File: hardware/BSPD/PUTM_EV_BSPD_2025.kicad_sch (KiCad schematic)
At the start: 27 parts, among them K1 Fujitsu_FTR-LYCA005x, Q1 NMOS, U1 MC78M12CDTG, U10 4069, U2 LM1117IMP-5.0, U4 Opamp_Dual, U5 4081

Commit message: Crumbs of documentation added
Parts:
- R1: value R -> 10k
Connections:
- net at C7.1, R18.2, R19.1: no longer U10.1
- net SCS Loop but the other side: now reaches K1.11
- net SCS Loop: now reaches K1.14
- no-connect marks 0 -> 3
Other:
- note added: "(Labels will be changed to not idiotic)"
- note added: "...eventually"
- note added: "0.5V-4.5V Output Comparator"
- note added: "A nice little graph of trigger times + voltages will be added"
- note added: "Comparator will be added here"
- note added: "Timing Section 500ms Charge 10s Discharge"
- moved on the sheet: C7, R18, R19, R3, R5, U10A, U5A

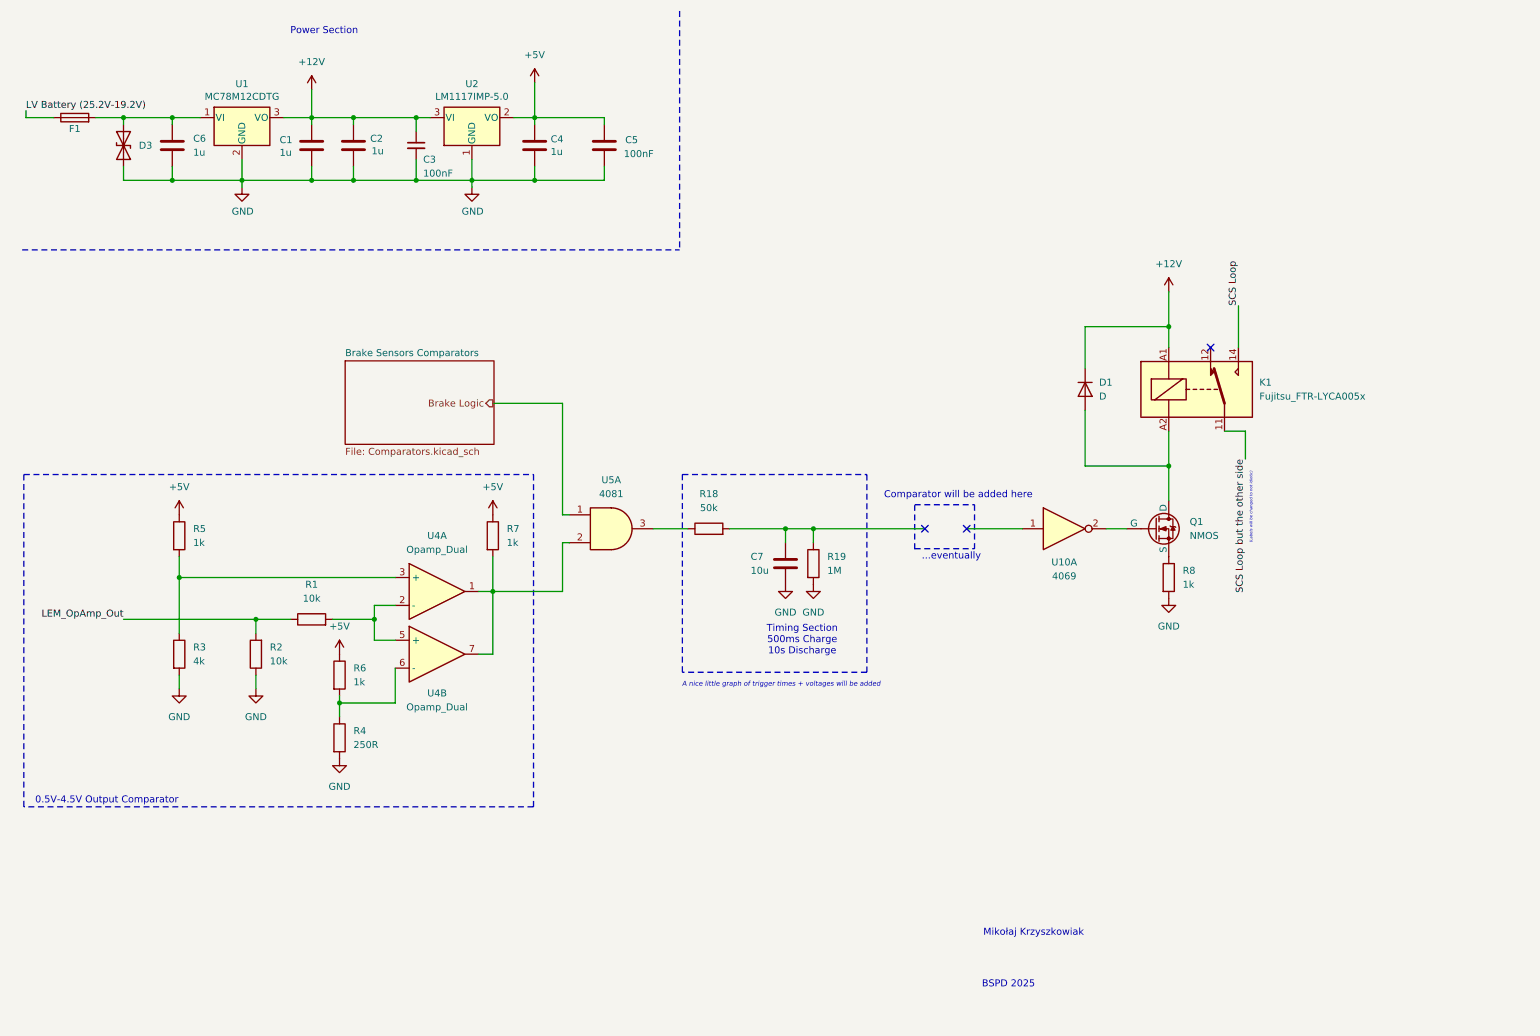
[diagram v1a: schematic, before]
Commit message: Timing Changed + Documented
Changed 10 second autoreset timer to a 555 in one-shot configuration. Also documented BSPD Board.
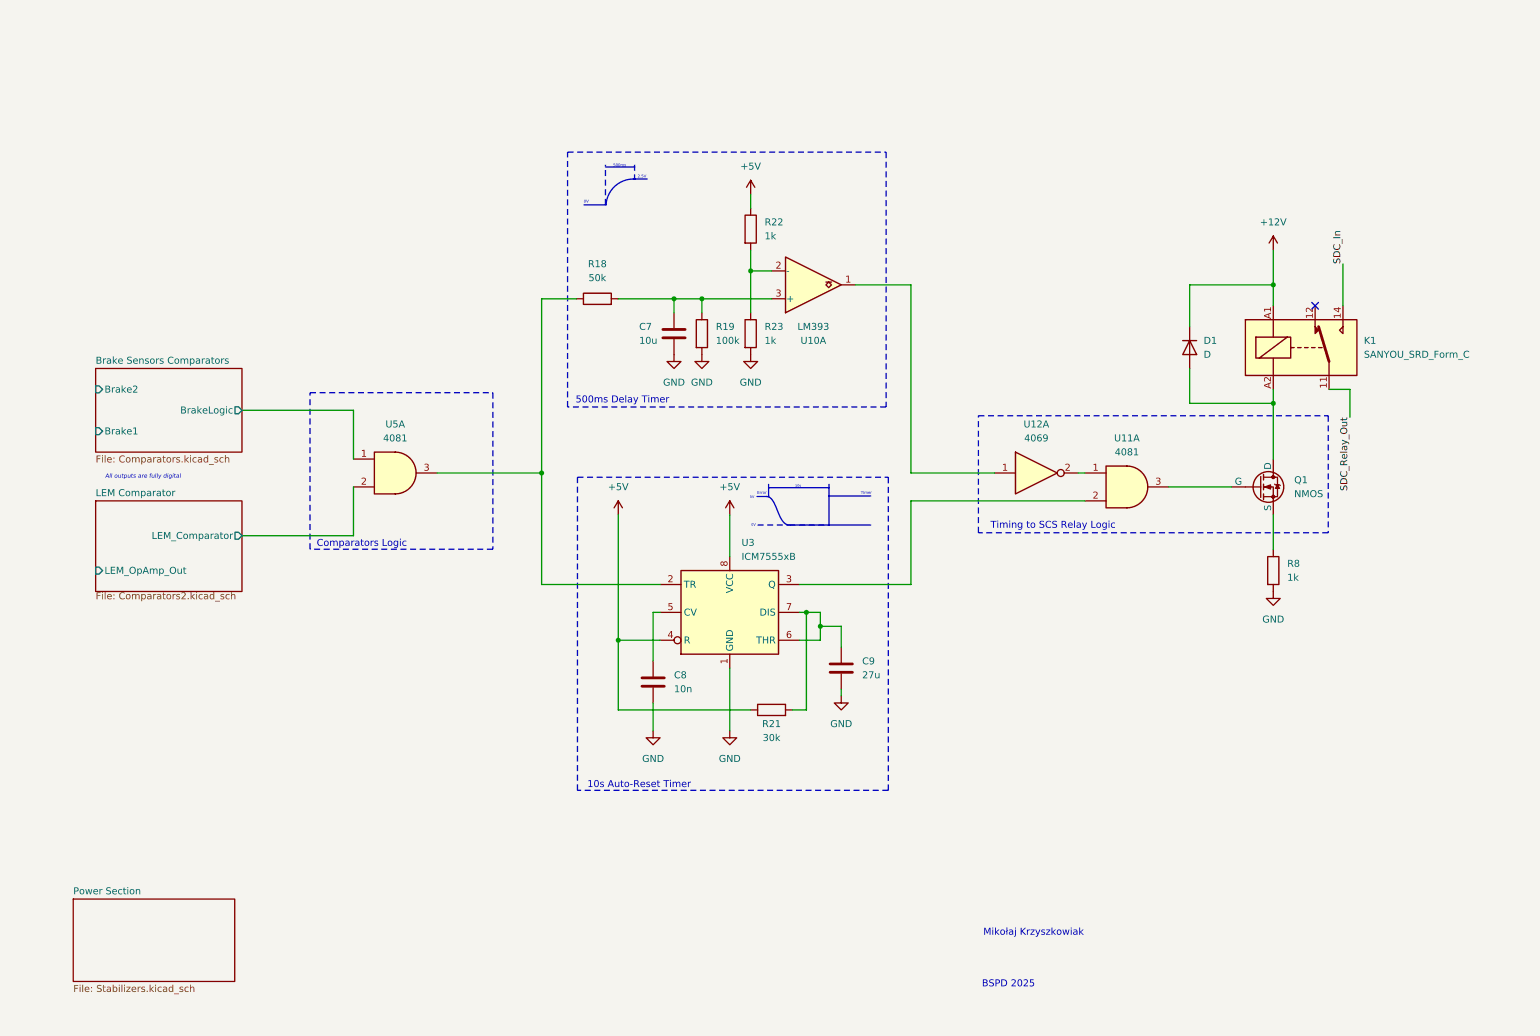
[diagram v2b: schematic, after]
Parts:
- removed C1, C2, C4: 1u, Capacitor_SMD:C_0805_2012Metric, symbol PUTM_EV_IMD_SAFETY_2021-rescue:C-Device
- removed C3: 100nF, Capacitor_SMD:C_0603_1608Metric, symbol Device:C_Small
- removed C5: 100nF, Capacitor_SMD:C_0603_1608Metric, symbol PUTM_EV_IMD_SAFETY_2021-rescue:C-Device
- removed C6: 1u, symbol Device:C
- removed D3: 1N630xCA, Diode_THT:D_DO-201AE_P15.24mm_Horizontal, symbol Diode:1N630xCA
- removed F1: 500mA, symbol Device:Fuse
- removed R1: 10k, symbol Device:R
- removed R2: 10k, Resistor_SMD:R_1206_3216Metric, symbol Device:R
- removed R3: 4k, symbol Device:R
- removed R4: 250R, symbol Device:R
- removed R5, R6, R7: 1k, symbol Device:R
- removed U1: MC78M12CDTG, Package_TO_SOT_SMD:TO-252-3_TabPin2, symbol PUTM_EV_IMD_SAFETY_2021-rescue:MC78M05_TO252-Regulator_Linear
- removed U10: 4069, symbol 4xxx:4069
- removed U2: LM1117IMP-5.0, Package_TO_SOT_SMD:SOT-223-3_TabPin2, symbol PUTM_EV_IMD_SAFETY_2021-rescue:LM1117-5.0-Regulator_Linear
- removed U4: Opamp_Dual, symbol Device:Opamp_Dual
- added C8: 10n, symbol Device:C
- added C9: 27u, symbol Device:C
- added R21: 30k, symbol Device:R
- added R22, R23: 1k, symbol Device:R
- added U10: LM393, symbol Comparator:LM393
- added U11: 4081, symbol 4xxx:4081
- added U12: 4069, symbol 4xxx:4069
- added U3: ICM7555xB, Package_SO:SOIC-8_3.9x4.9mm_P1.27mm, symbol Timer:ICM7555xB
- K1: value Fujitsu_FTR-LYCA005x -> SANYOU_SRD_Form_C
- R19: value 1M -> 100k
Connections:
- net +5V: now also R21.1, R22.1, U3.4 (R), U3.8 (VCC)
- net GND: now also C8.2, C9.2, R23.2, U3.1 (GND)
- net at C7.1, R18.2, R19.1: now also U10.3 (+)
- net at R18.1, U5.3: now also U3.2 (TR)
- net at Q1.2 (G): now also U11.3
- net LEM Comparator/LEM_Comparator: now reaches U5.2
- net Brake Logic renamed Brake Sensors Comparators/BrakeLogic
- net SCS Loop renamed SDC_In
- net SCS Loop but the other side renamed SDC_Relay_Out
- new net: R22.2, R23.1, U10.2 (-)
- new net: C9.1, R21.2, U3.6 (THR), U3.7 (DIS)
- new net: U11.2, U3.3 (Q)
- new net: C8.1, U3.5 (CV)
- new net: U10.1, U12.1
- new net: U11.1, U12.2
- no-connect marks 3 -> 1
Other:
- added sheet LEM Comparator (Comparators2.kicad_sch)
- added sheet Power Section (Stabilizers.kicad_sch)
- sheet Brake Sensors Comparators ports: added Brake1, Brake2, BrakeLogic; removed none
- note added: "0V"
- note added: "10s"
- note added: "10s Auto-Reset Timer"
- note added: "2.5V"
- note added: "500ms"
- note added: "500ms Delay Timer"
- note added: "5V"
- note added: "All outputs are fully digital"
- note added: "Comparators Logic"
- note added: "Error"
- note added: "Timer"
- note added: "Timing to SCS Relay Logic"
- note removed: "(Labels will be changed to not idiotic)"
- note removed: "...eventually"
- note removed: "0.5V-4.5V Output Comparator"
- note removed: "A nice little graph of trigger times + voltages will be added"
- note removed: "Comparator will be added here"
- note removed: "Power Section"
- note removed: "Timing Section 500ms Charge 10s Discharge"
- moved on the sheet: C7, D1, K1, Q1, R18, R19, R8, U5A

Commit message: Minor documentation + schematic changes
Changed documentation to more descriptive, fixed zajebas where OpAmps were placed instead of comparators. 
Changed resistors values on CS board
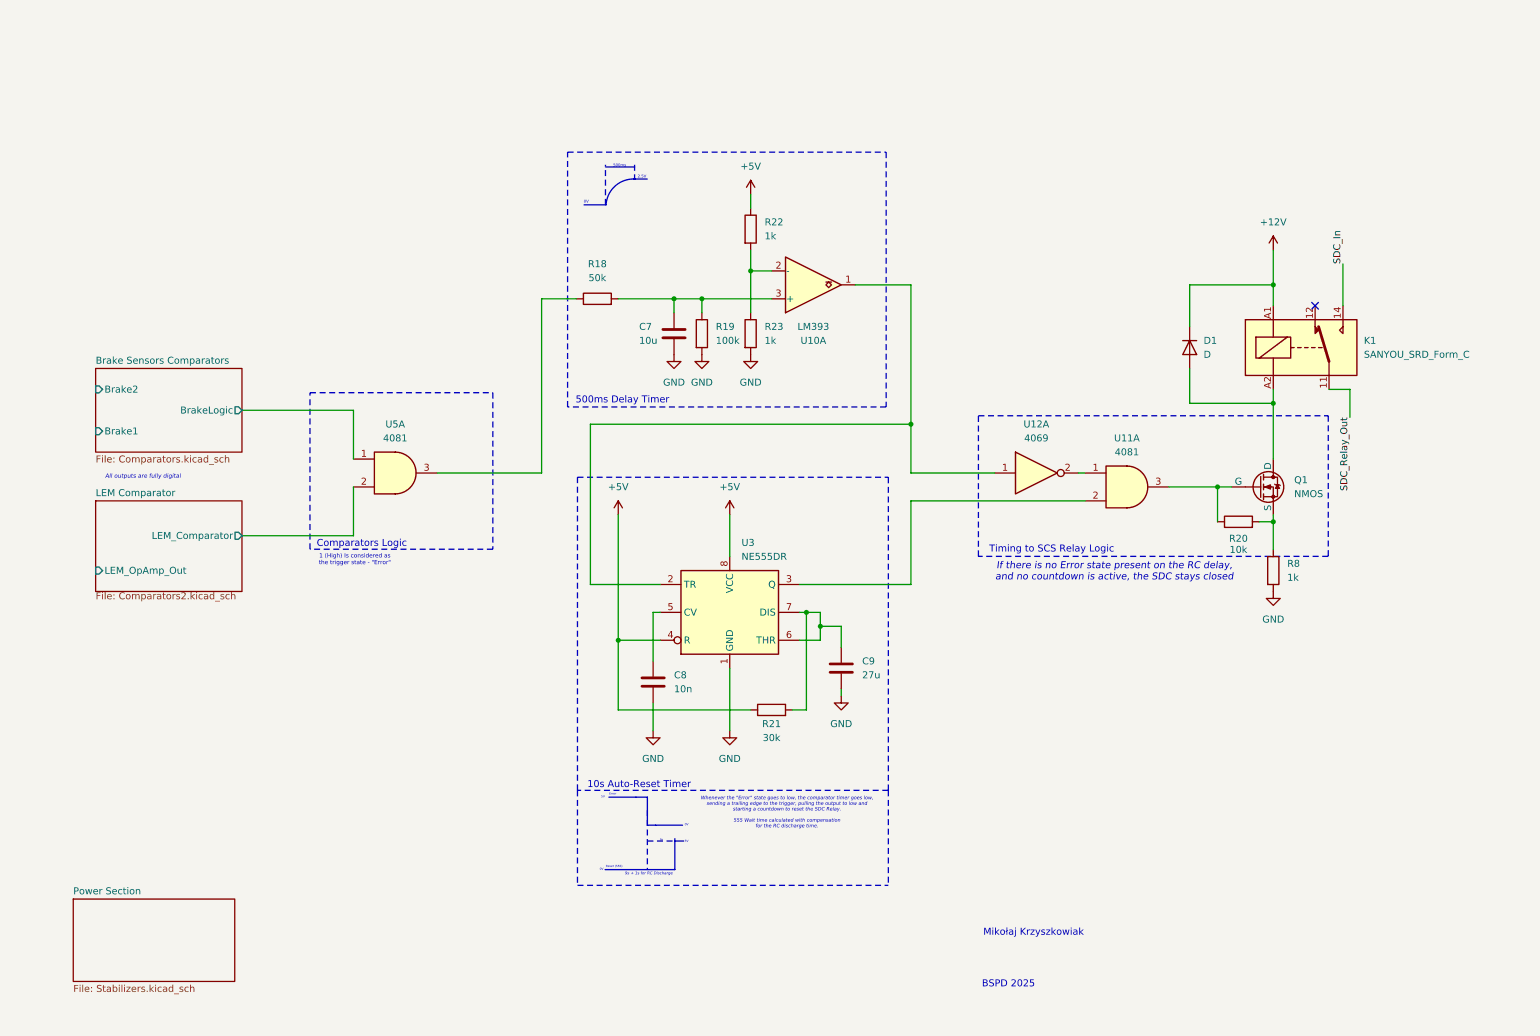
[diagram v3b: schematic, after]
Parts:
- added R20: 10k, symbol Device:R
- U3: value ICM7555xB -> NE555DR
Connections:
- net at R18.1, U5.3: no longer U3.2 (TR)
- net at U10.1, U12.1: now also U3.2 (TR)
- net at Q1.2 (G), U11.3: now also R20.1
- net at Q1.3 (S), R8.1: now also R20.2
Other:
- note added: "1 (High) Is considered as the trigger state - "Error""
- note added: "9s"
- note added: "9s + 1s for RC Discharge"
- note added: "If there is no Error state present on the RC delay, and no countdown is active, the SDC stays closed"
- note added: "Reset (555)"
- note added: "Whenever the "Error" state goes to low, the comparator timer goes low, sending a trailing edge to the trigger, pulling the output to low and starting a countdown to reset the SDC Relay. 555 Wait time calculated with compensation for the RC discharge time."
- note removed: "10s"
- note removed: "Timer"

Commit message: Fixed logic errors + assigned element values
Fixed wrong logic on Brake Sensor comparators, assigned IC's and connectors, added TVS diodes on connectors.
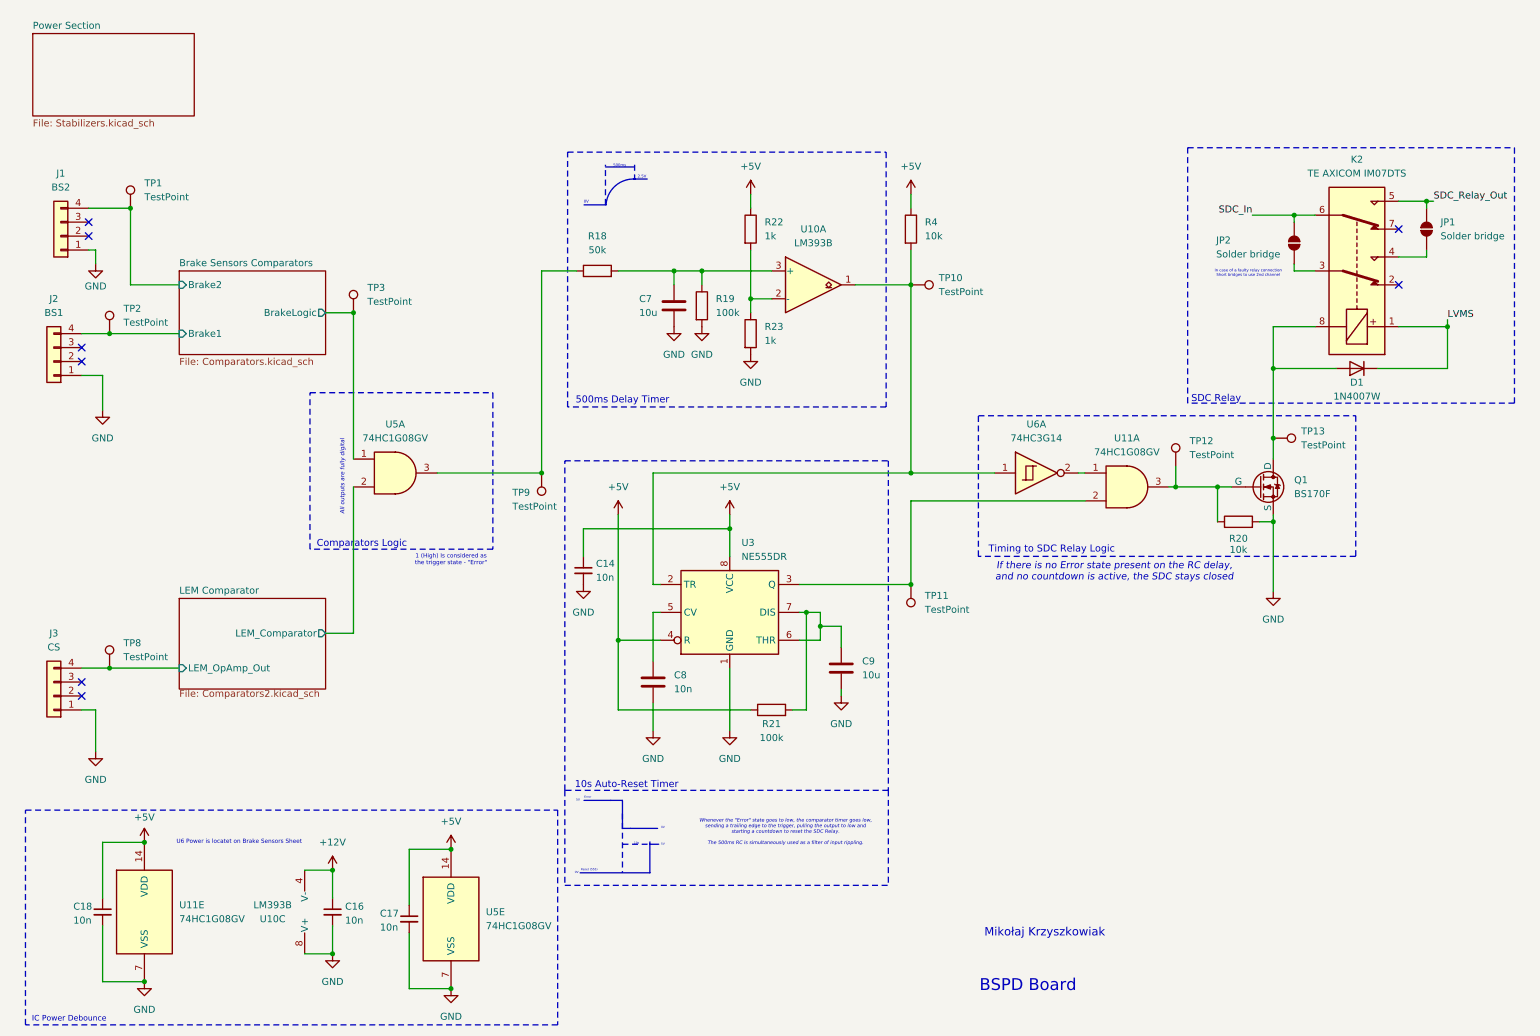
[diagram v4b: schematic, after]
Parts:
- removed K1: SANYOU_SRD_Form_C, Relay_THT:Relay_SPDT_Fujitsu_FTR-LYCA005x_FormC_Vertical, symbol Relay:Fujitsu_FTR-LYCA005x
- removed R8: 1k, symbol Device:R
- removed U12: 4069, symbol 4xxx:4069
- added C14, C16, C17, C18: 10n, symbol Device:C_Small
- added J1: BS2, symbol Connector_Generic:Conn_01x04
- added J2: BS1, symbol Connector_Generic:Conn_01x04
- added J3: CS, symbol Connector_Generic:Conn_01x04
- added JP1, JP2: Solder bridge, symbol Jumper:SolderJumper_2_Open
- added K2: TE AXICOM IM07DTS, footprints:IM23TS, symbol Relay:IM07
- added R4: 10k, symbol Device:R
- added TP1, TP10, TP11, TP12, TP13, TP2, TP3, TP8, TP9: TestPoint, symbol Connector:TestPoint
- added unit 3 of U10
- added unit 5 of U11
- added unit 5 of U5
- added U6: 74HC3G14, symbol 74xx:74HC14
- C9: value 27u -> 10u
- D1: value D -> 1N4007W
- Q1: value NMOS -> BS170F
- R21: value 30k -> 100k
- U10: value LM393 -> LM393B
- U11, U5: value 4081 -> 74HC1G08GV
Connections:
- net +12V: now also C16.1, U10.4 (V-); no longer D1.1 (K)
- net +5V: now also C14.1, C17.1, C18.1, R4.1, U11.14 (VDD), U5.14 (VDD)
- net Brake Sensors Comparators/Brake1: now also J2.4 (Pin_4), TP2.1
- net Brake Sensors Comparators/Brake2: now also J1.4 (Pin_4), TP1.1
- net Brake Sensors Comparators/BrakeLogic: now also TP3.1
- net GND: now also Q1.3 (S), R20.2, C14.2, C16.2, C17.2, C18.2, J1.1 (Pin_1), J2.1 (Pin_1), J3.1 (Pin_1), U10.8 (V+), U11.7 (VSS), U5.7 (VSS)
- net LEM Comparator/LEM_OpAmp_Out: now also J3.4 (Pin_4), TP8.1
- net SDC_In: now also JP2.2 (B), K2.6
- net SDC_Relay_Out: now also JP1.2 (B), K2.5
- net at Q1.2 (G), R20.1, U11.3: now also TP12.1
- net at R18.1, U5.3: now also TP9.1
- net at U10.1, U3.2 (TR): now also R4.2, TP10.1, U6.1
- net at U11.2, U3.3 (Q): now also TP11.1
- net at U11.1: now also U6.2
- net at D1.2 (A), Q1.1 (D): now also K2.8, TP13.1
- new net: JP2.1 (A), K2.3
- new net: JP1.1 (A), K2.4
- new net LVMS: D1.1 (K), K2.1
- no-connect marks 1 -> 8
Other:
- note added: "10s"
- note added: "BSPD Board"
- note added: "IC Power Debounce"
- note added: "In case of a faulty relay connection Short bridges to use 2nd channel"
- note added: "SDC Relay"
- note added: "Timing to SDC Relay Logic"
- note added: "U6 Power is locatet on Brake Sensors Sheet"
- note added: "Whenever the "Error" state goes to low, the comparator timer goes low, sending a trailing edge to the trigger, pulling the output to low and starting a countdown to reset the SDC Relay. The 500ms RC is simultaneously used as a filter of input rippling."
- note removed: "9s"
- note removed: "9s + 1s for RC Discharge"
- note removed: "BSPD 2025"
- note removed: "Timing to SCS Relay Logic"
- note removed: "Whenever the "Error" state goes to low, the comparator timer goes low, sending a trailing edge to the trigger, pulling the output to low and starting a countdown to reset the SDC Relay. 555 Wait time calculated with compensation for the RC discharge time."
- moved on the sheet: C7, D1, R18, R19
